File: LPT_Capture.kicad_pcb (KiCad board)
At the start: 2 copper layers, 22 x 36 mm, 9 parts, among them J1 USB_B_Micro, J2 DB25 Male, U1 FT245RL

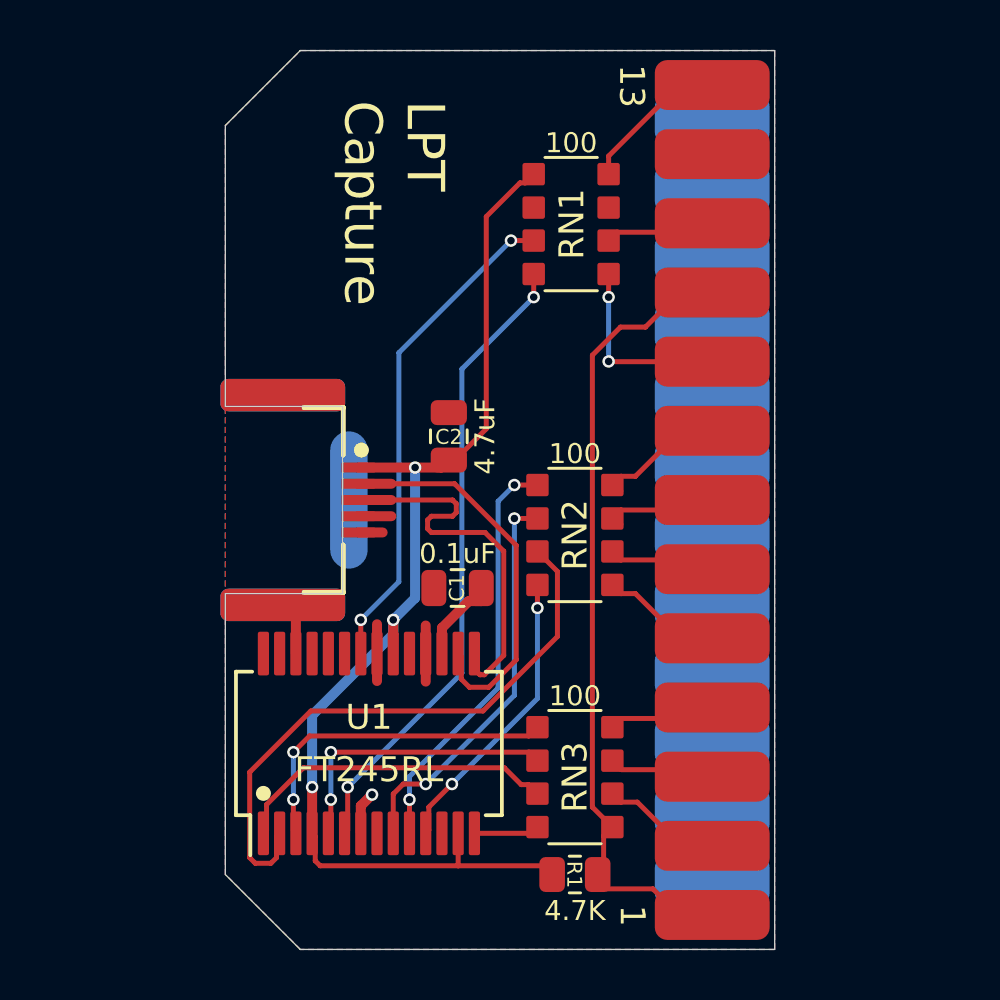
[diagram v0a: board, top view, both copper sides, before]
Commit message: v004 rn footprints, add fb1 c3 c4
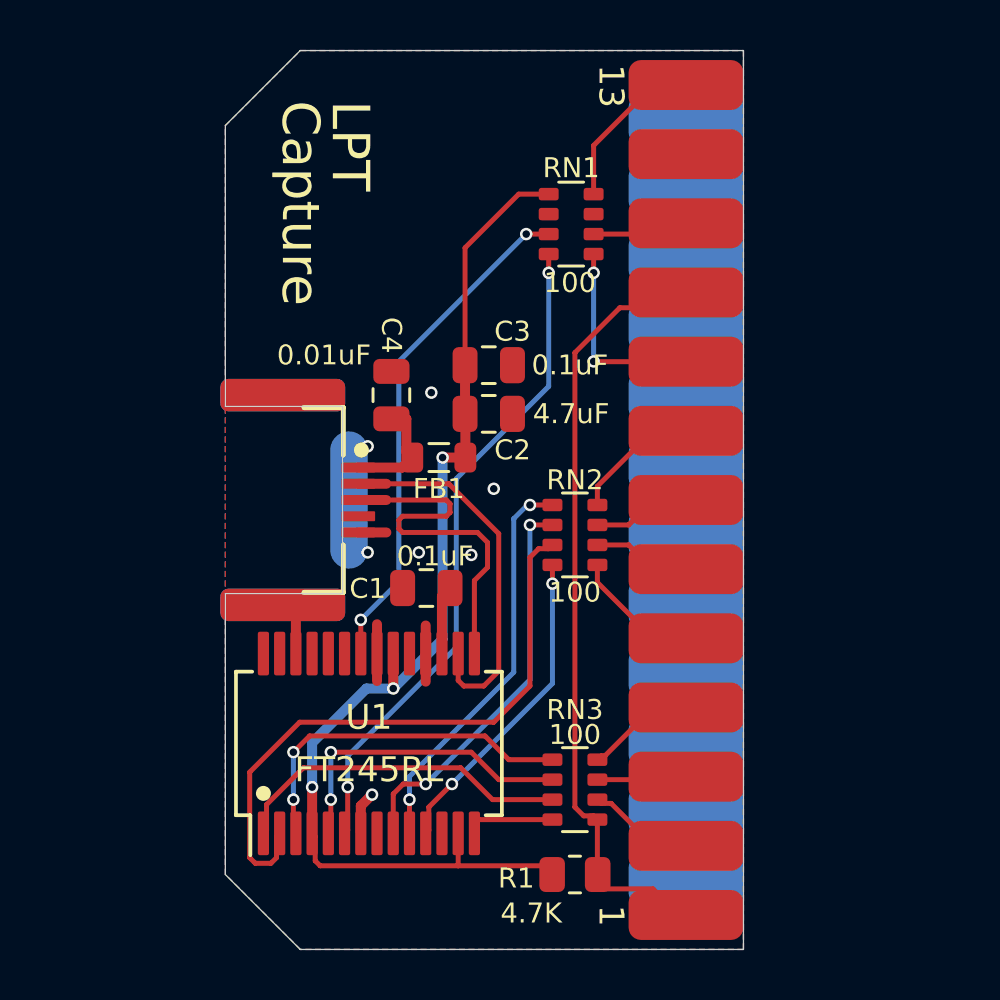
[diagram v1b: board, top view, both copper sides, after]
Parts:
- added C3: 0.1uF, 000_LOCAL:C_0805_2012Metric, F.Cu at (149.6, 94.6)
- added C4: 0.01uF, 000_LOCAL:C_0805_2012Metric, F.Cu at (145.7, 95.8)
- added FB1: MI0805K400R-10, 000_LOCAL:L_0805_2012Metric, F.Cu at (147.6, 98.3)
- RN1, RN2, RN3: footprint 000_LOCAL:R_Array_Convex_4x1206 -> 000_LOCAL:R_Array_Convex_4x0603
- moved C2 1.84 mm to (149.6, 96.5), turned to 0 degrees
- moved C1 1.25 mm to (147.1, 103.5)
- moved J2 1.05 mm to (157.9, 100.0)
- moved RN3 0.50 mm to (153.0, 111.6)
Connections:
- J1 pad 1: VCC -> VBUS
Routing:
- net VBUS: track 0.00 -> 4.58 mm
- net VCC: track 46.7 -> 45.0 mm
- net /PD7: track 7.65 -> 9.05 mm
- net (no net): track 1.33 -> 0.00 mm
- net /D3: track 11.8 -> 12.9 mm
- net /D7: track 25.5 -> 26.6 mm
- net /USB-: track 15.8 -> 14.8 mm
- net /WR: track 2.63 -> 3.57 mm
- net /USB+: track 15.8 -> 14.9 mm
- net /D1: track 11.7 -> 12.6 mm
- net /D2: track 13.5 -> 14.3 mm
- net /PD5: track 4.80 -> 3.96 mm
- net /3v3: track 3.57 -> 2.76 mm
- net /D0: track 13.1 -> 13.8 mm
- net /PD1: track 4.27 -> 3.60 mm
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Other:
- board size 22 x 36 mm -> 20.8 x 36 mm
- board text added: "v004"
- board text removed: "v003"

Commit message: bom & readme
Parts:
- moved C3 10.5 mm to (147.1, 104.8), turned to 90 degrees
- moved C2 9.39 mm to (145.1, 104.8), turned to 90 degrees
- moved C1 2.35 mm to (149.0, 104.8), turned to 270 degrees
- moved U1 1.76 mm to (145.8, 111.2)
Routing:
- net /~TXE: track 20.4 -> 28.9 mm, vias 2 -> 0
- net GND: track 12.7 -> 16.5 mm, vias 7 -> 6
- net VCC: track 45.0 -> 48.6 mm
- net /D1: track 12.6 -> 10.7 mm
- net /D0: track 13.8 -> 12.4 mm
- net /~STROBE: track 32.6 -> 31.3 mm
- net /USB-: track 14.8 -> 16.1 mm
- net /USB+: track 14.9 -> 16.1 mm
- net /D4: track 24.6 -> 25.8 mm
- net /D2: track 14.3 -> 13.2 mm
- net /D3: track 12.9 -> 13.9 mm
- net /PD7: track 9.05 -> 8.00 mm
- net /D7: track 26.6 -> 27.6 mm
- net /D6: track 16.1 -> 17.1 mm
- net /D5: track 16.0 -> 17.1 mm
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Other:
- board text added: "v005"
- board text removed: "v004"

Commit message: minor layout nudges
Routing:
- net (no net): track 0.00 -> 1.12 mm
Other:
- board text added: "v006"
- board text removed: "v005"

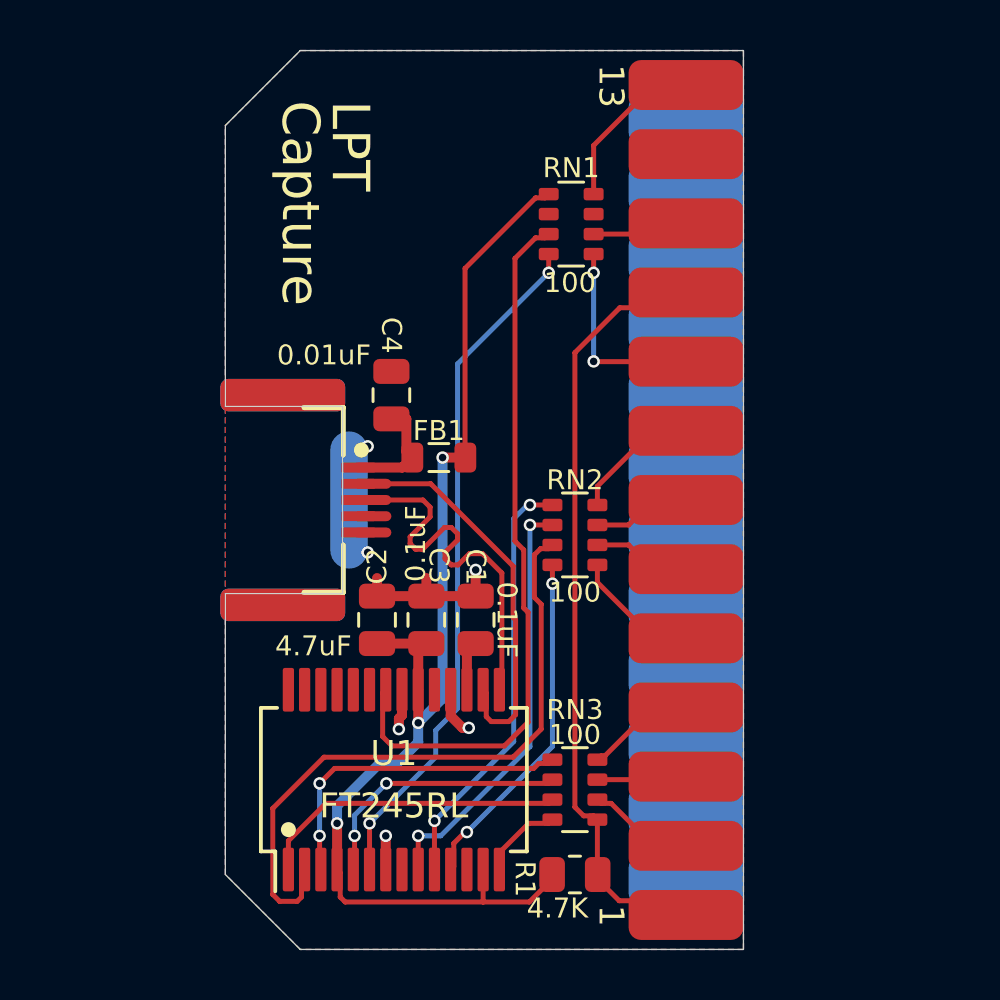
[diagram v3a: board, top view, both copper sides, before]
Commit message: better usb port attachment
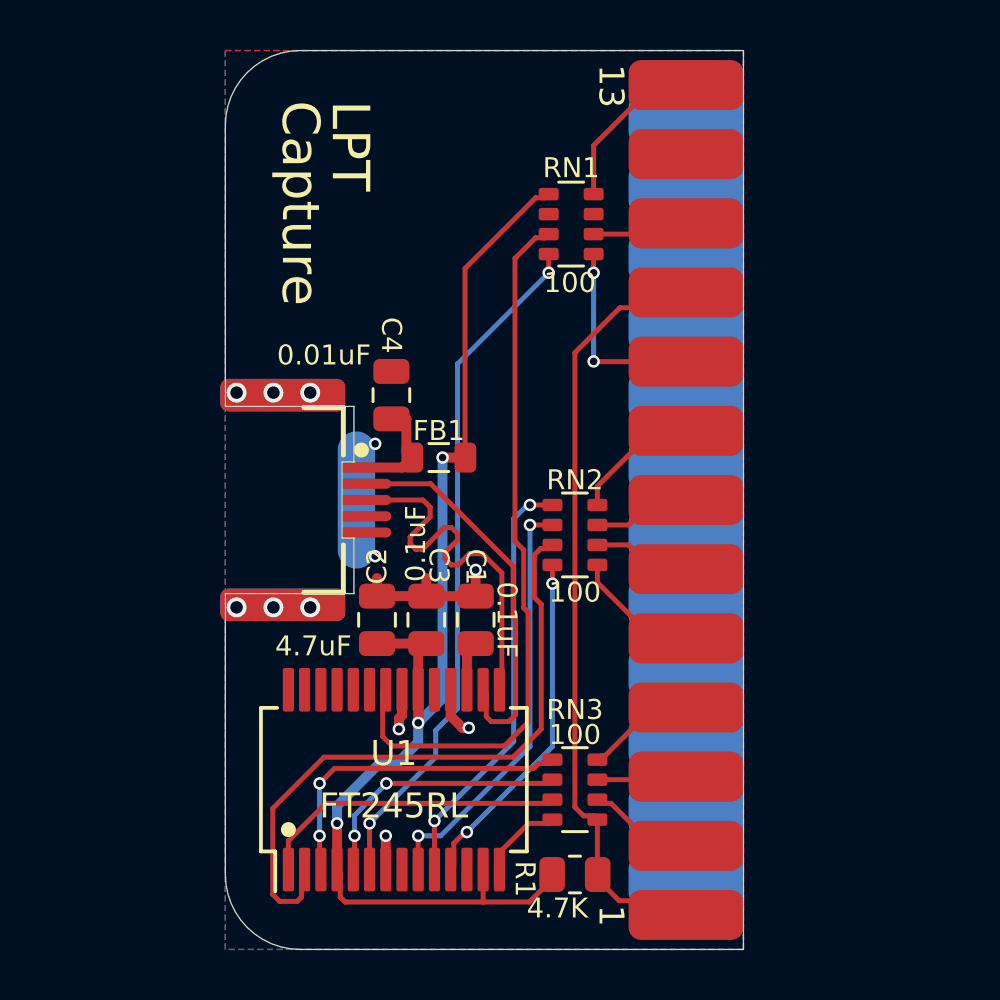
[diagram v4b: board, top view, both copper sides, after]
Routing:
- net GND: vias 6 -> 12
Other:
- outline, holes or cut-outs redrawn
- board text added: "v007"
- board text removed: "v006"

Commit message: v008, better usb port
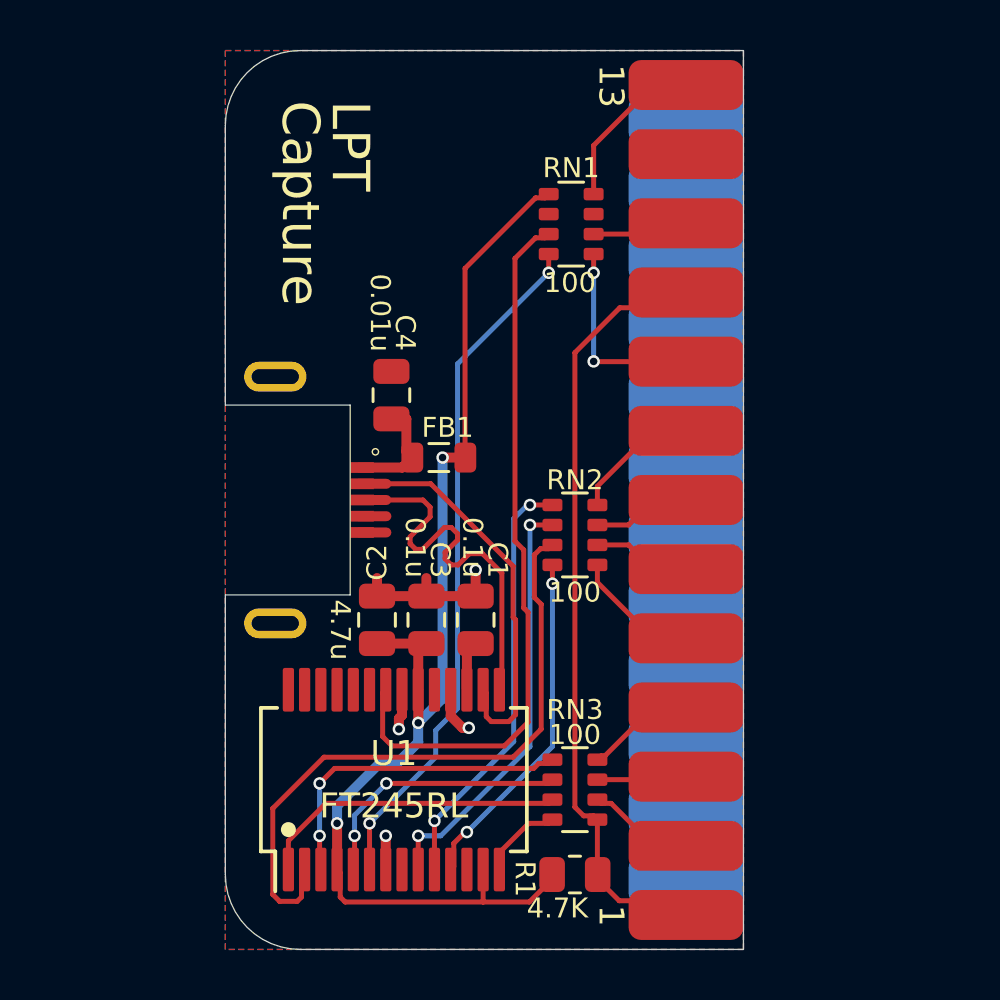
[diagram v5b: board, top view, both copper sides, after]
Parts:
- C1, C3: value 0.1uF -> 0.1u
- C2: value 4.7uF -> 4.7u
- C4: value 0.01uF -> 0.01u
- FB1: value MI0805K400R-10 -> 40 Ohm 1.5A
- J1: value USB_B_Micro -> USB3155-XX-X_REVA; footprint 000_LOCAL:GCT_USB3100-XX-X_inverted -> 000_LOCAL:GCT_USB3155-XX-X_REVA
- moved J1 0.05 mm to (141.0, 100.0)
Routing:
- net GND: track 16.5 -> 12.5 mm, vias 12 -> 4
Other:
- outline, holes or cut-outs redrawn

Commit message: version silkscreen
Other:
- board text added: "v008"
- board text removed: "v007"

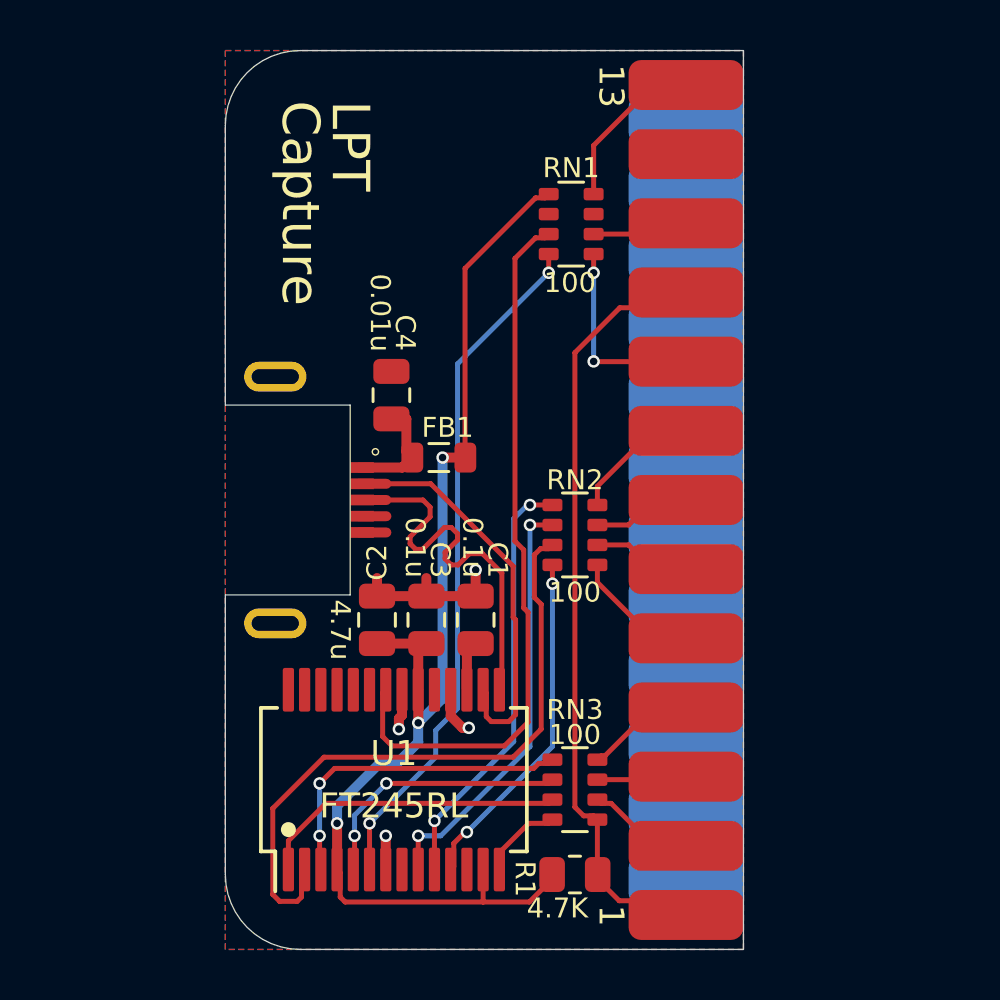
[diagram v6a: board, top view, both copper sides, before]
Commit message: disconnect Select
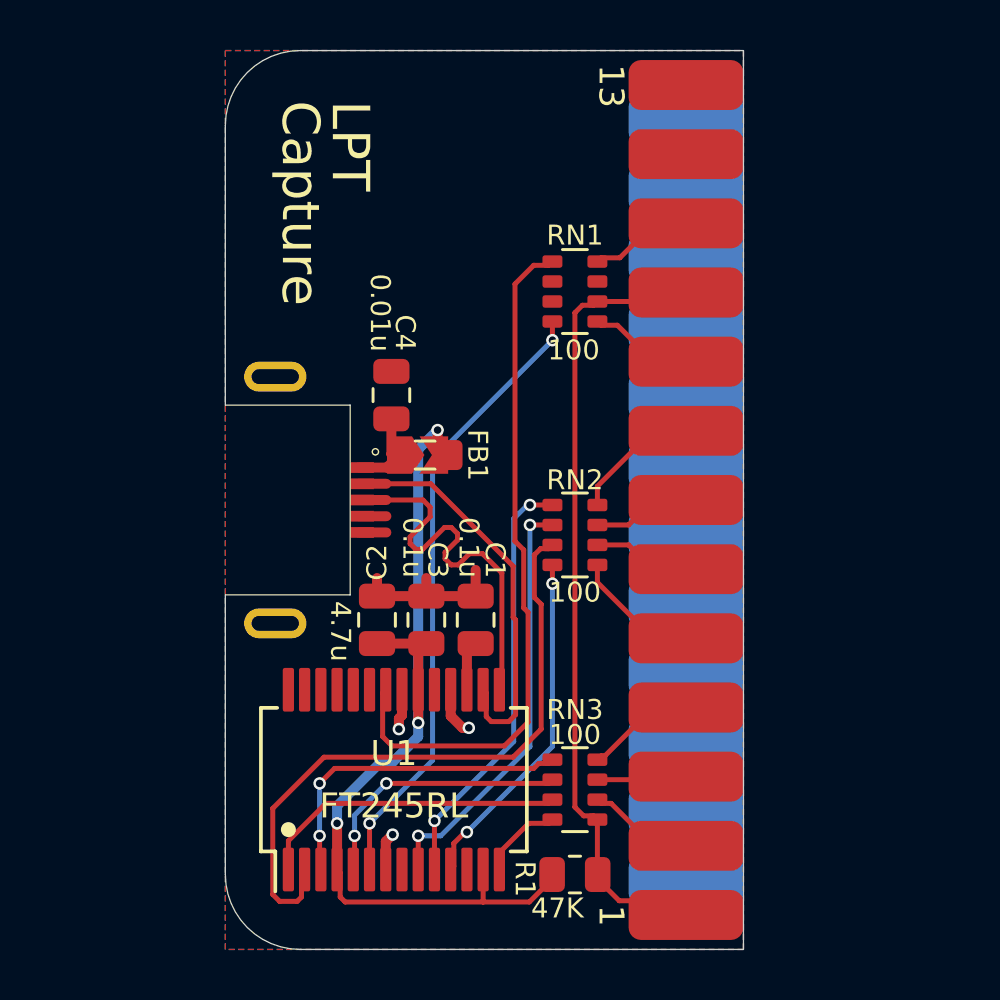
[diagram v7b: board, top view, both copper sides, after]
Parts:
- added JP1: SolderJumper_2_Open, 000_LOCAL:SolderJumper-2_P1.3mm_Open_TrianglePad1.0x1.5mm, F.Cu at (146.7, 98.2)
- FB1: value 40 Ohm 1.5A -> 40-1.5A
- R1: value 4.7K -> 47K
- moved RN1 2.70 mm to (153.0, 91.7)
- moved FB1 0.56 mm to (147.0, 98.2)
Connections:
- J2 pad 11: /~BUSY -> /BUSY
- J2 pad 13: /Select -> (no net)
- RN1 pad 1: VCC -> /~TXE
- RN1 pad 3: /~TXE -> (no net)
- RN1 pad 6: /~BUSY -> /~STROBE
- RN1 pad 8: /Select -> /BUSY
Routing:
- net VCC: track 48.6 -> 38.3 mm
- net /Select: track 6.65 -> 0.00 mm
- net /BUSY: track 0.00 -> 4.18 mm
- net /~BUSY: track 3.88 -> 0.00 mm
- net /PD7: track 8.00 -> 4.22 mm, vias 2 -> 0
- net /D7: track 27.6 -> 25.0 mm
- net VBUS: track 4.58 -> 3.61 mm
- net /~STROBE: track 31.3 -> 32.2 mm
- net /~TXE: track 28.8 -> 27.9 mm
- net GND: track 12.5 -> 12.7 mm, vias 4 -> 3
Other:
- board text added: "v009"
- board text removed: "v008"

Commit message: kicad 6, minor layout tweaks, ft245rl symbol
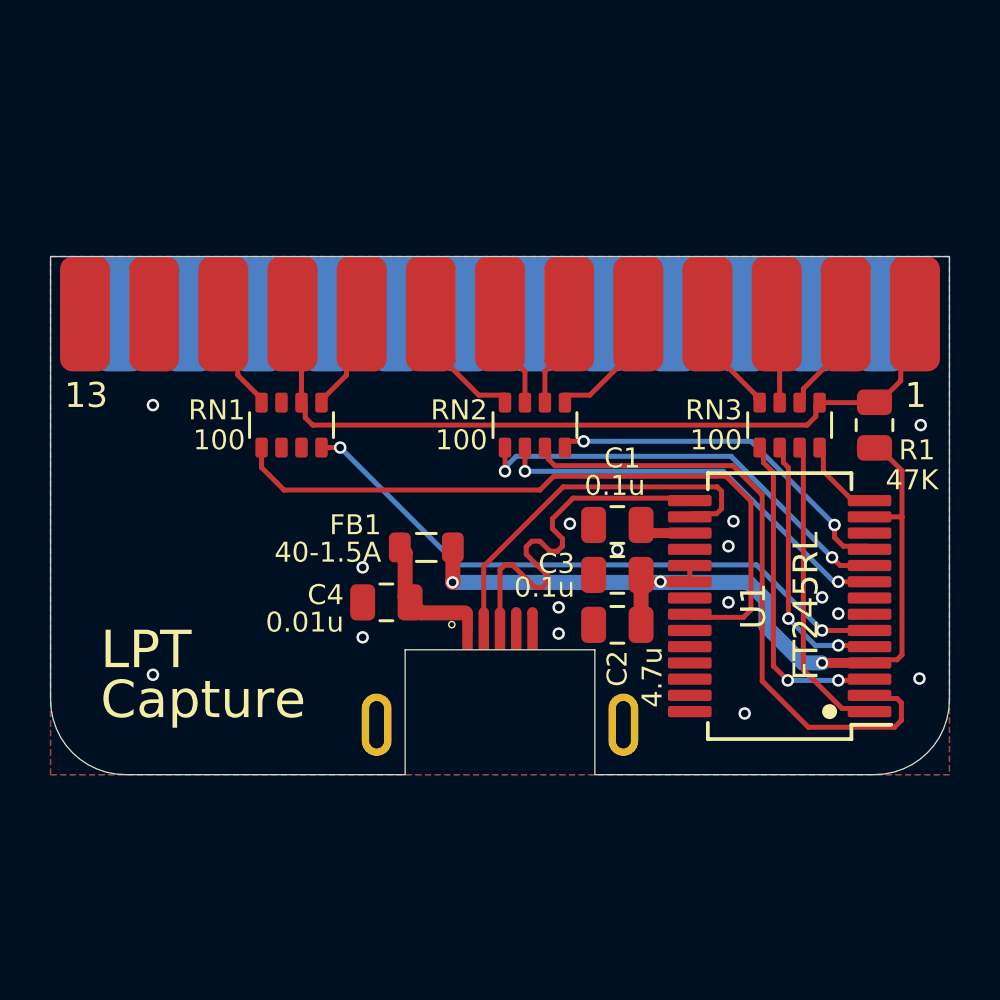
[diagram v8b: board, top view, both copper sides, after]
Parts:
- removed JP1: SolderJumper_2_Open, 000_LOCAL:SolderJumper-2_P1.3mm_Open_TrianglePad1.0x1.5mm
- moved R1 21.6 mm to (165.0, 97.0), turned to -90 degrees
- moved RN3 16.9 mm to (161.6, 97.0), turned to 90 degrees
- moved U1 16.9 mm to (161.2, 104.2), turned to 180 degrees
- moved J1 12.7 mm to (150.0, 109.0), turned to 0 degrees
- moved RN1 12.5 mm to (141.7, 97.0), turned to 90 degrees
- moved J2 11.2 mm to (150.0, 92.0), turned to 180 degrees
- moved C2 9.63 mm to (154.7, 105.0), turned to 180 degrees
- moved C4 8.30 mm to (145.4, 104.1), turned to 180 degrees
- moved C3 7.86 mm to (154.7, 103.0), turned to 180 degrees
- moved C1 6.83 mm to (154.7, 101.0), turned to 0 degrees
- moved RN2 4.68 mm to (151.4, 97.0), turned to 90 degrees
- moved FB1 3.70 mm to (147.1, 101.9), turned to 0 degrees
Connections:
- net /~STROBE renamed /~{STROBE}
- net /~TXE renamed /~{TXE}
- FB1 pad 1: VCC -> VBUS
- FB1 pad 2: VBUS -> VCC
- J1 pad 4: (no net) -> unconnected-(J1-Pad4)
- J2 pad 13: (no net) -> /Select
- J2 pad 14: (no net) -> /~{AutoLineFeed}
- J2 pad 17: (no net) -> /~{Select-Printer}
- RN1 pad 3: (no net) -> unconnected-(RN1-Pad3)
- U1 pad 12: (no net) -> unconnected-(U1-Pad12)
- U1 pad 19: (no net) -> VCC
- U1 pad 23: (no net) -> unconnected-(U1-Pad23)
- U1 pad 27: (no net) -> unconnected-(U1-Pad27)
- U1 pad 28: (no net) -> unconnected-(U1-Pad28)
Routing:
- net GND: track 12.7 -> 0.00 mm, vias 3 -> 16
- net VCC: track 38.3 -> 36.4 mm
- net VBUS: track 3.61 -> 5.52 mm
- net (no net): track 1.12 -> 0.00 mm
- net /D3: track 13.9 -> 14.5 mm
- net /D6: track 17.1 -> 17.7 mm
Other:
- board size 20.8 x 36 mm -> 36 x 20.8 mm
- net class Default removed
- net class USB Data removed
- board text added: "${TITLE} ${REVISION} ${COMMENT2}"
- board text removed: "github.com/bkw777/LPT_Capture"
- board text removed: "v009"
